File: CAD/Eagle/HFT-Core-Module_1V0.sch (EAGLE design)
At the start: 399 parts, among them Q0521 ABS07-32.768KHZ, Q0811 ABM03B-32.000MHZ, Q0911 ABM3B-16MHZ-10-R50-1-U, T1201 MMBT2222, T1202 MMBT2222, T1203 MMBT2222, U0111 STM32L4Z_144PIN_SMPS, U0431 PAM2305AAB120, U0601 LM4120IM5-3.0, U0611 MAX5217, U0631 CFPT-141-20MHZ, U0641 OPA354, U0701 Si5338, U0801 SX1276, U0901 AX5243, U0911 PE4259, U0921 PE4259, U0991 PE4259, U1101 MCP3911A0-E-SS, U1111 MAX5136AGTG+, U1121 OPA354, U1131 OPA354, U1141 OPA354, U1201 NHD-C0220BIZ_2X20CHARS, U1301 MPU-9250, U1311 MS5607-02BA03, U1321 SHT31-DIS, U1401 SOLARPANEL_3V3_5MA1_25MM_X_20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, U1402 SPV1040T, U1501 TS5A23166, U1601 SC189ZSKTRT, U1701 TS5A23166, U1801 TS5A23166, U1901 TS5A23166, X1261 TTE_EN11-HSM, X2001 MOLEX 105017-0001, X2101 SMA_SMT_AMPHENOL-901-143, SAM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, X2111 SMA_SMT_AMPHENOL-901-143, SAM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, X2201 CUI SJ1-3535NS, X2211 CUI SJ1-3535NS, X2311 2X20/90_1MM27_HARWIN_M50-3202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, X2312 2X20/90_1MM27_HARWIN_M50-3202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, X2321 2X20/90_1MM27_HARWIN_M50-3202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, X2322 2X20/90_1MM27_HARWIN_M50-3202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, X2331 2X20/90_1MM27_HARWIN_M50-3202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, X2332 2X20/90_1MM27_HARWIN_M50-3202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

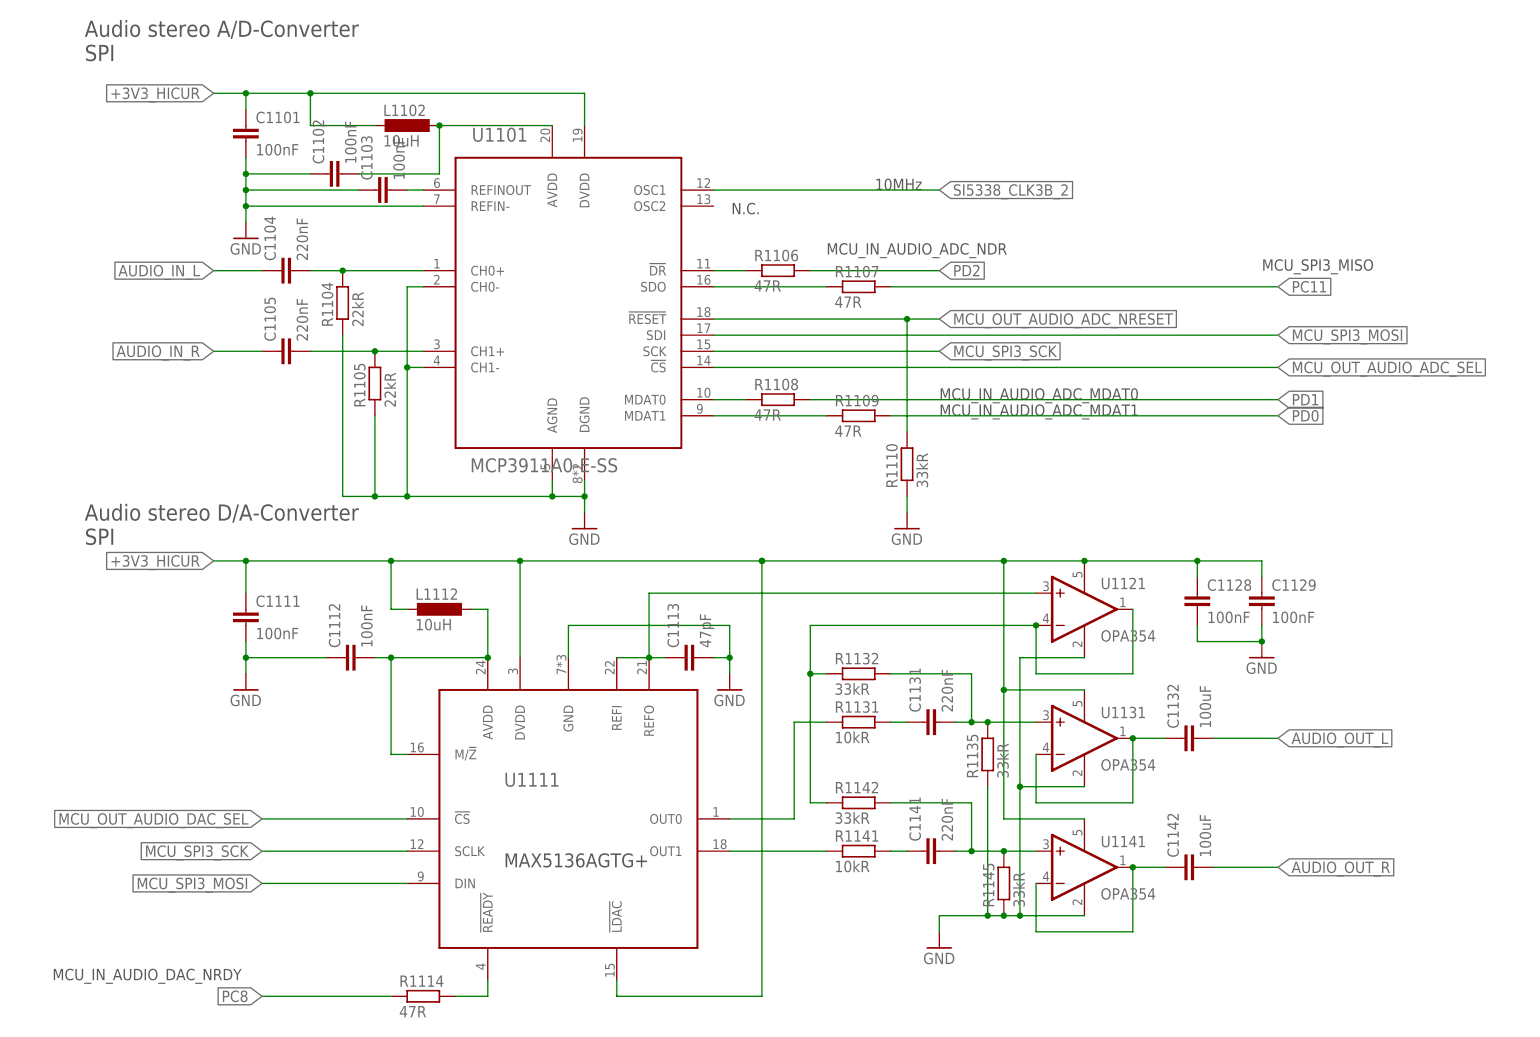
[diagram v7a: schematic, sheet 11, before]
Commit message: HW_1V0 - ADC resistor values changed, ADC OSC2 should be connected to GND (reminder added)
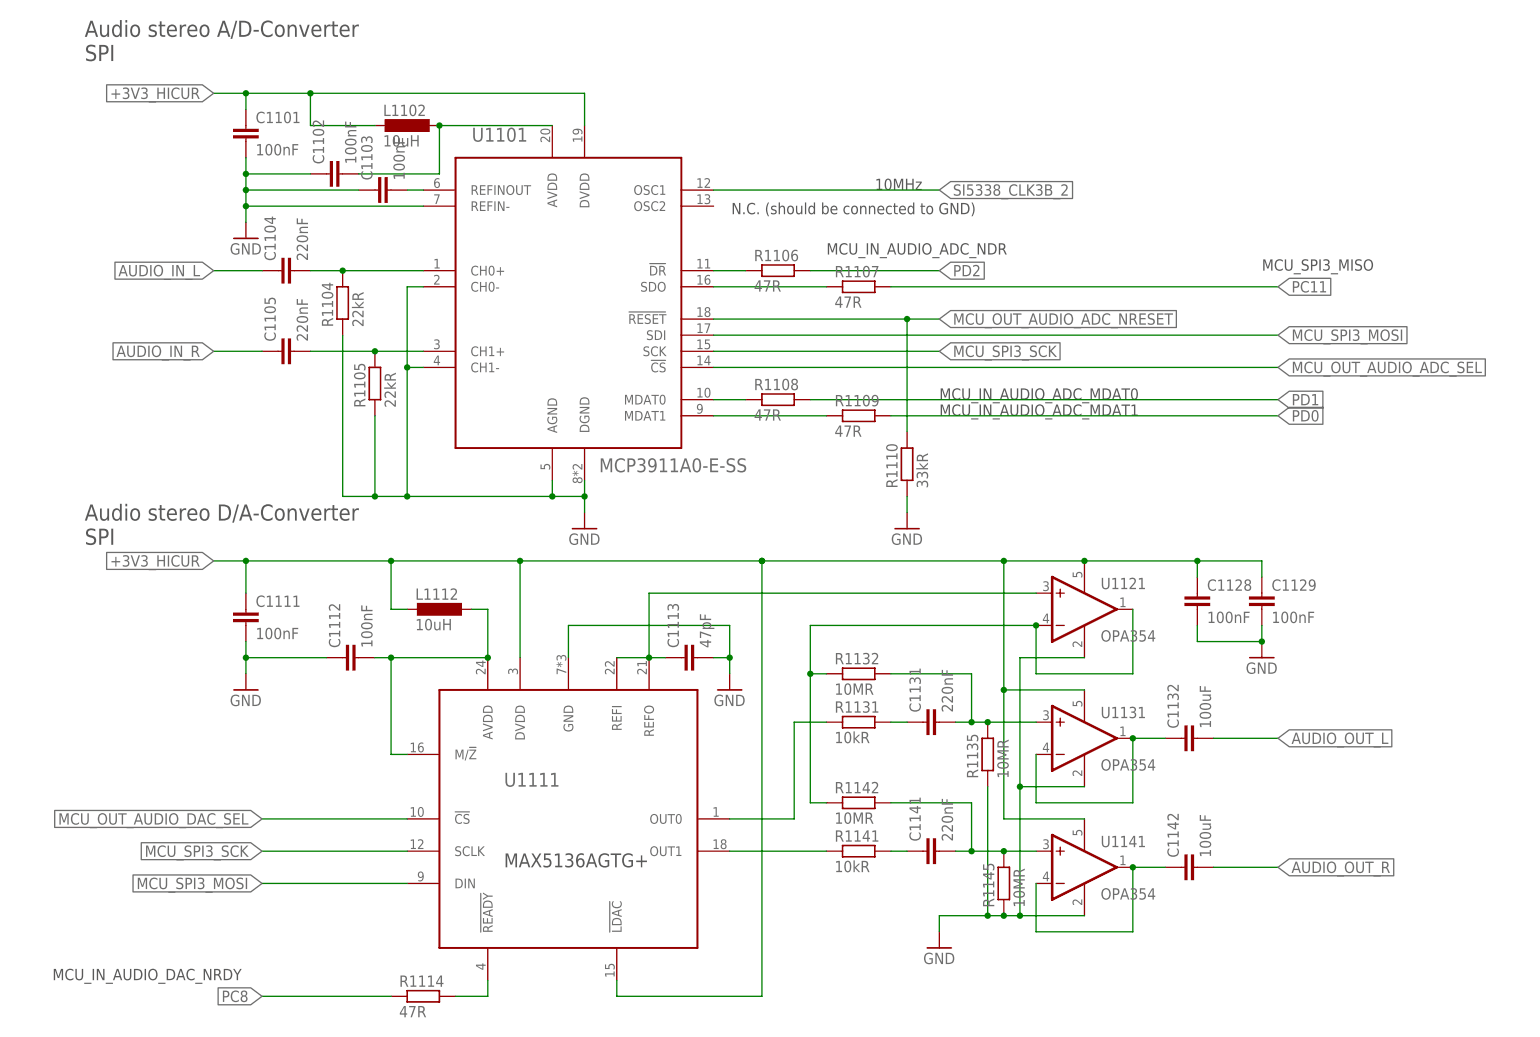
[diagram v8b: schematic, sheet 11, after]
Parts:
- R1132, R1135, R1142, R1145: value 33kR -> 10MR
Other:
- note added: "N.C. (should be connected to GND)"
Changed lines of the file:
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@@
 <part name="C1112" library="rcl" deviceset="C-EU" device="C0603" value="100nF"/>
 <part name="R1114" library="rcl" deviceset="R-EU_" device="R0603" value="47R"/>
-<part name="R1132" library="rcl" deviceset="R-EU_" device="R0603" value="33kR"/>
-<part name="R1142" library="rcl" deviceset="R-EU_" device="R0603" value="33kR"/>
+<part name="R1132" library="rcl" deviceset="R-EU_" device="R0603" value="10MR"/>
+<part name="R1142" library="rcl" deviceset="R-EU_" device="R0603" value="10MR"/>
 <part name="R1131" library="rcl" deviceset="R-EU_" device="R0603" value="10kR"/>
 <part name="R1141" library="rcl" deviceset="R-EU_" device="R0603" value="10kR"/>
@@
 <part name="C1131" library="df4iah_rcl" deviceset="C-EU" device="C0603" value="220nF"/>
 <part name="GND1121" library="df4iah_supply" deviceset="GND" device=""/>
-<part name="R1135" library="rcl" deviceset="R-EU_" device="R0603" value="33kR"/>
-<part name="R1145" library="rcl" deviceset="R-EU_" device="R0603" value="33kR"/>
+<part name="R1135" library="rcl" deviceset="R-EU_" device="R0603" value="10MR"/>
+<part name="R1145" library="rcl" deviceset="R-EU_" device="R0603" value="10MR"/>
 <part name="GND1102" library="df4iah_supply" deviceset="GND" device=""/>
 <part name="U1101" library="df4iah_adc" deviceset="MCP3911" device="" value="MCP3911A0-E-SS"/>
@@
 <text x="22.86" y="162.56" size="2.54" layer="97" ratio="15">Audio stereo A/D-Converter
 SPI</text>
-<text x="124.714" y="138.43" size="1.778" layer="97">N.C.</text>
+<text x="124.714" y="138.43" size="1.778" layer="97">N.C. (should be connected to GND)</text>
 <text x="147.32" y="142.24" size="1.778" layer="97">10MHz</text>
 <text x="22.86" y="86.36" size="2.54" layer="97" ratio="15">Audio stereo D/A-Converter
@@
 <instance part="R1145" gate="G$1" x="167.64" y="33.02" rot="R90"/>
 <instance part="GND1102" gate="1" x="101.6" y="88.9"/>
-<instance part="U1101" gate="G$1" x="99.06" y="124.46"/>
+<instance part="U1101" gate="G$1" x="99.06" y="124.46" smashed="yes">
+<attribute name="NAME" x="83.82" y="149.86" size="2.1844" layer="95" ratio="10"/>
+<attribute name="VALUE" x="103.886" y="97.79" size="2.1844" layer="96" ratio="10"/>
+</instance>
 <instance part="R1106" gate="G$1" x="132.08" y="129.54"/>
 <instance part="R1107" gate="G$1" x="144.78" y="127"/>
